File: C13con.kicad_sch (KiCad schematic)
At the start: 21 parts, among them J2 DCC connector, J3 EDG connector, J4 Power Daisy Chain, J6 Power Daisy Chain, J7 Power Output, K1 G6K-2, Q1 BC848W

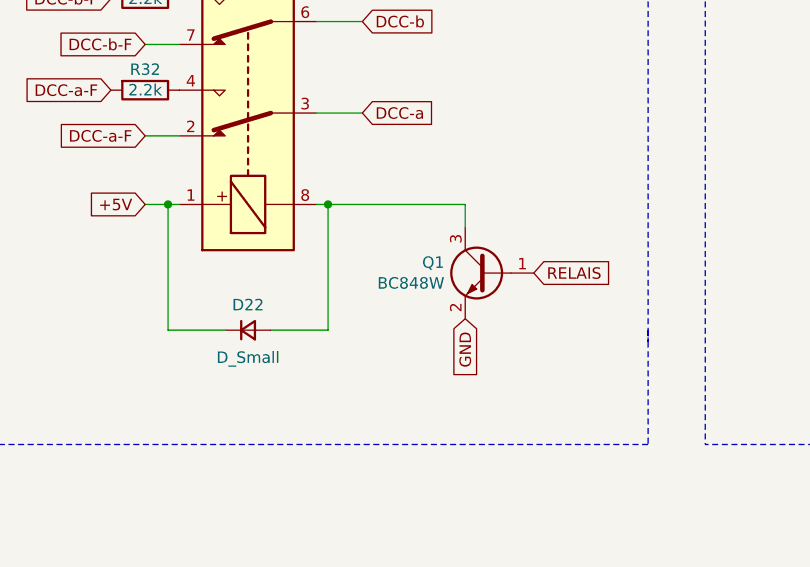
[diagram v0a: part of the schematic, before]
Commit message: mod: conversion to KiCad 9
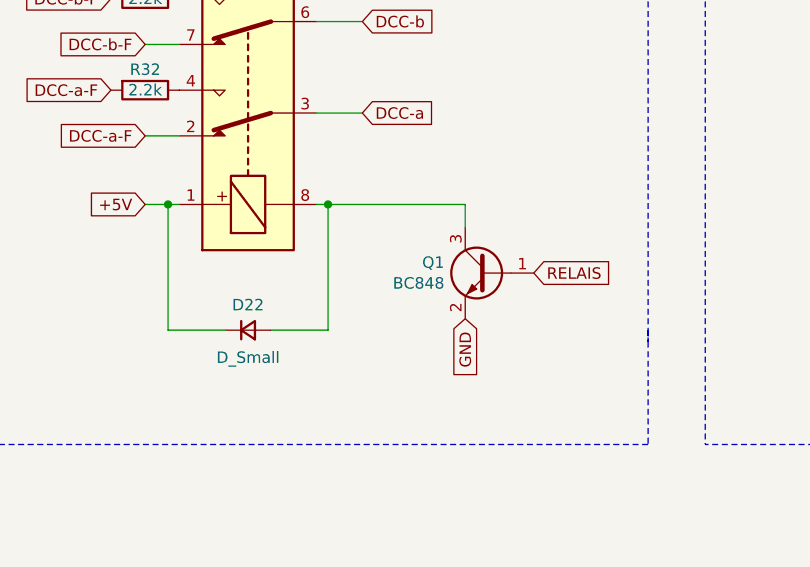
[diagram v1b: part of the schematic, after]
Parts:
- Q1: value BC848W -> BC848; LCSC Part # C549496 -> C600677
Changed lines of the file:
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@@
 	(title_block
 		(title "RTB C13 Module")
-		(date "2023-10-25")
-		(rev "1")
+		(date "2025-10-14")
+		(rev "2")
 		(company "Frank Schumacher")
 		(comment 1 "Track Sensor")
@@
 			)
 		)
-		(property "Value" "BC848W"
+		(property "Value" "BC848"
 			(at 100.5586 133.223 0)
 			(effects
@@
 			)
 		)
-		(property "Description" "100MHz 100mA 110@2mA,5V 15nA 200mV 200mW 30V 5V NPN SOT-323 Bipolar (BJT) ROHS"
+		(property "Description" "-65℃~+150℃ 100mA 100nA 200@2mA,5V 200MHz 200mW 250mV 30V NPN SOT-323 Bipolar (BJT) ROHS"
 			(at 105.41 132.08 0)
 			(effects
@@
 			)
 		)
-		(property "LCSC Part #" "C549496"
+		(property "LCSC Part #" "C600677"
 			(at 105.41 132.08 0)
 			(effects
